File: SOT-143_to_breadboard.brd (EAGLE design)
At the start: 5.1 x 10.2 mm, 3 parts, among them J1 CONNECTOR_2, J2 CONNECTOR_2-NO_SQUARE, U1 MAX6315US29D2-T

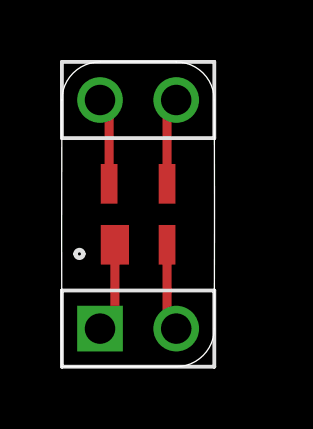
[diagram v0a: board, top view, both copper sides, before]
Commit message: fixed SOT-143 board - previous version was 0.200" wide, and OSH Park requires boards to be 0.250" or more on X and Y dimensions.  So it has a vestigal PCB extension of 0.050" on the right side.
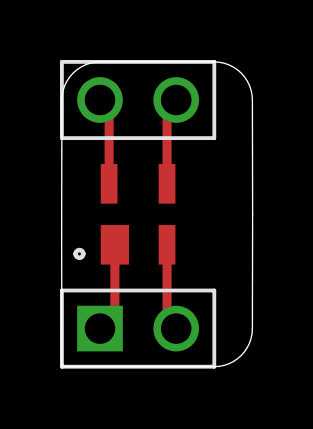
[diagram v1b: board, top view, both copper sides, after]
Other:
- board size 5.1 x 10.2 mm -> 6.4 x 10.2 mm
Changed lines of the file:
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@@
 <board>
 <plain>
-<wire x1="3.81" y1="10.16" x2="1.29" y2="10.16" width="0" layer="20"/>
-<wire x1="3.81" y1="10.16" x2="5.08" y2="8.89" width="0" layer="20" curve="-89.661374"/>
-<wire x1="5.08" y1="8.89" x2="5.08" y2="1.27" width="0" layer="20" curve="-0.436592"/>
-<wire x1="5.08" y1="1.27" x2="3.81" y2="0" width="0" layer="20" curve="-89.661515"/>
-<wire x1="0" y1="0" x2="3.79" y2="0" width="0" layer="20"/>
+<wire x1="5.08" y1="10.16" x2="1.29" y2="10.16" width="0" layer="20"/>
+<wire x1="5.08" y1="10.16" x2="6.35" y2="8.89" width="0" layer="20" curve="-89.661374"/>
+<wire x1="6.35" y1="8.89" x2="6.35" y2="1.27" width="0" layer="20" curve="-0.436592"/>
+<wire x1="6.35" y1="1.27" x2="5.08" y2="0" width="0" layer="20" curve="-89.661515"/>
+<wire x1="0" y1="0" x2="5.06" y2="0" width="0" layer="20"/>
 <wire x1="0" y1="0" x2="0" y2="8.89" width="0" layer="20" curve="-0.472974"/>
 <wire x1="0" y1="8.89" x2="1.27" y2="10.16" width="0" layer="20" curve="-89.661515"/>
-<text x="2.54" y="5.08" size="0.9398" layer="22" font="vector" ratio="10" rot="MR270" align="center">SnapEDA
+<text x="3.175" y="5.08" size="0.9652" layer="22" font="vector" ratio="10" rot="MR180" align="center">SnapEDA
 SOT-143</text>
 </plain>
